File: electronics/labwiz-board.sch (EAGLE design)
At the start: 129 parts, among them IC1 MCP3424, J1 SD_MICRO_SDIO_1BIT, J2 CORTEX_DEBUGSMD, J30 4P-SMD-2.0-90D, J4 4P-SMD-2.0-90D, J5 4P-SMD-2.0-90D, U1 STM32F10XRXT6, U4 MIC5219-3.3V, X2 M12_BOTTOM_CONTACTS_FPC_1MM, Y1 32.768kHz, Y3 32.768kHz

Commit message: Added a header for USART1 Rx Tx.
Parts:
- added J43: (no value), SparkFun-Connectors:M02PTH
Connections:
- net USART1_RX: now also J43.2
- net USART1_TX: now also J43.1
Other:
- note added: "0.1.2-beta"
- note added: "BL-5C Batt"
- note added: "NOTES - Add labels to SWD pogo pads - Move the Cortex debug header to the right spot - Implement battery charging - VBAT_1/2 and SD_DETECT can reused as output if throw on some diodes."
- note removed: "0.13"
- note removed: "BL-5C Battery"
- note removed: "NOTES - Add labels to SWD pogo pads - Move the Cortex debug header to the right spot - Implement battery charging"
- note removed: "Orphan Nets"

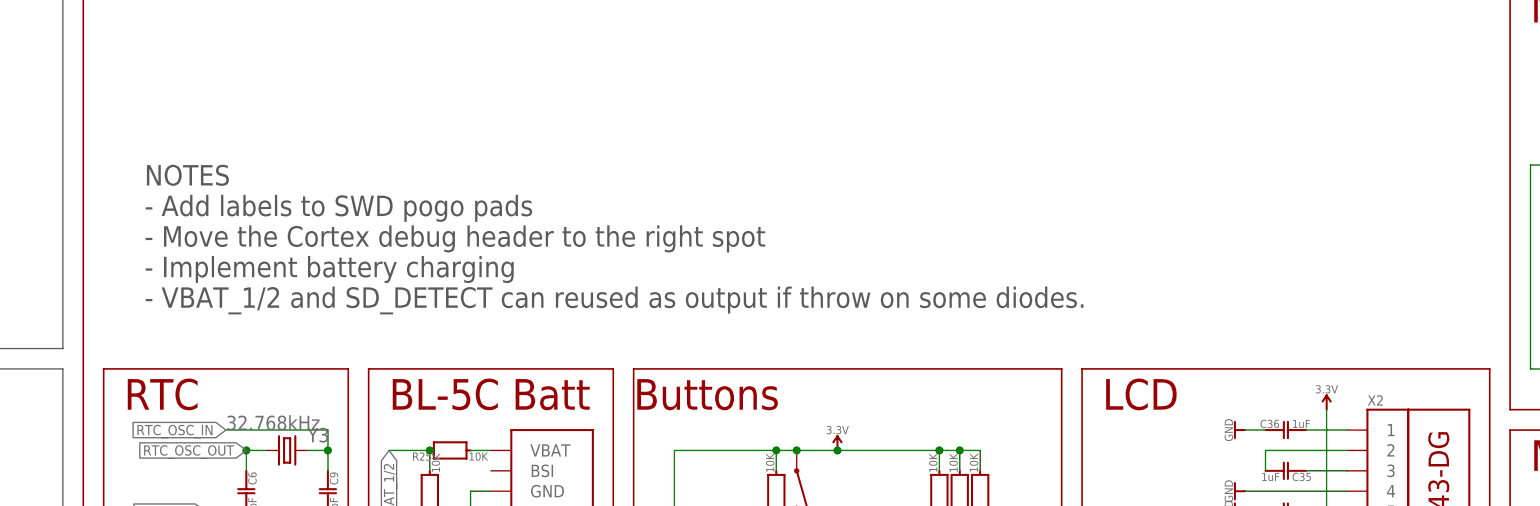
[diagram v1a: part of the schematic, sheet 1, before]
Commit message: Added pin docs to silk.
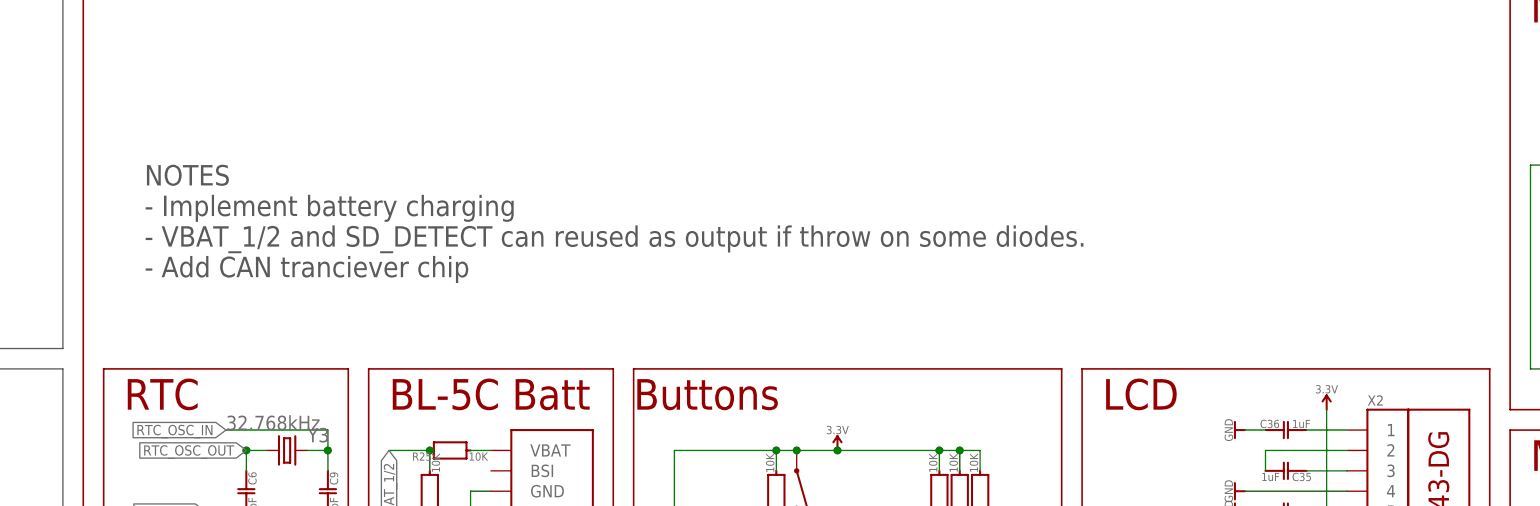
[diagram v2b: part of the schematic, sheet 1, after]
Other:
- note added: "NOTES - Implement battery charging - VBAT_1/2 and SD_DETECT can reused as output if throw on some diodes. - Add CAN tranciever chip"
- note removed: "NOTES - Add labels to SWD pogo pads - Move the Cortex debug header to the right spot - Implement battery charging - VBAT_1/2 and SD_DETECT can reused as output if throw on some diodes."
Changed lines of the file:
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@@
 <wire x1="289.56" y1="139.7" x2="381" y2="139.7" width="0.2032" layer="94"/>
 <text x="119.38" y="114.3" size="2.54" layer="97" align="top-left">NOTES
-- Add labels to SWD pogo pads
-- Move the Cortex debug header to the right spot
 - Implement battery charging
-- VBAT_1/2 and SD_DETECT can reused as output if throw on some diodes.</text>
+- VBAT_1/2 and SD_DETECT can reused as output if throw on some diodes.
+- Add CAN tranciever chip</text>
 <text x="193.04" y="22.86" size="1.27" layer="97" font="fixed" align="top-left">ESP01 Module
  TXO 2 1 GND

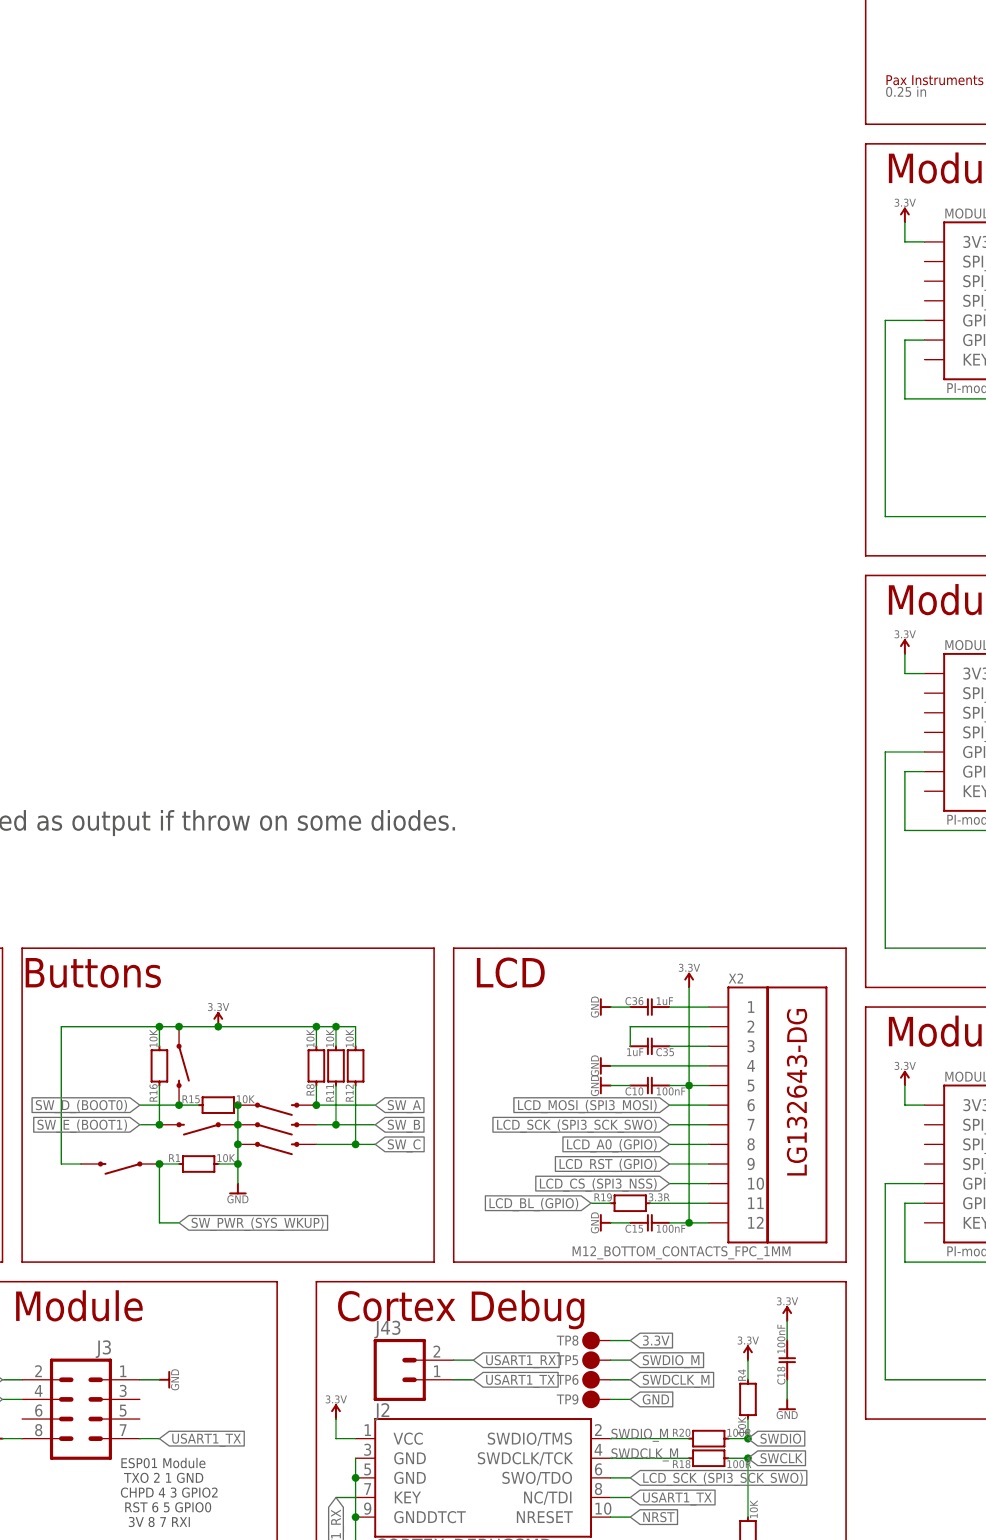
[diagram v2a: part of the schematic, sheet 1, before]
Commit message: Moved USART1. Added USART1 pullup resistors.
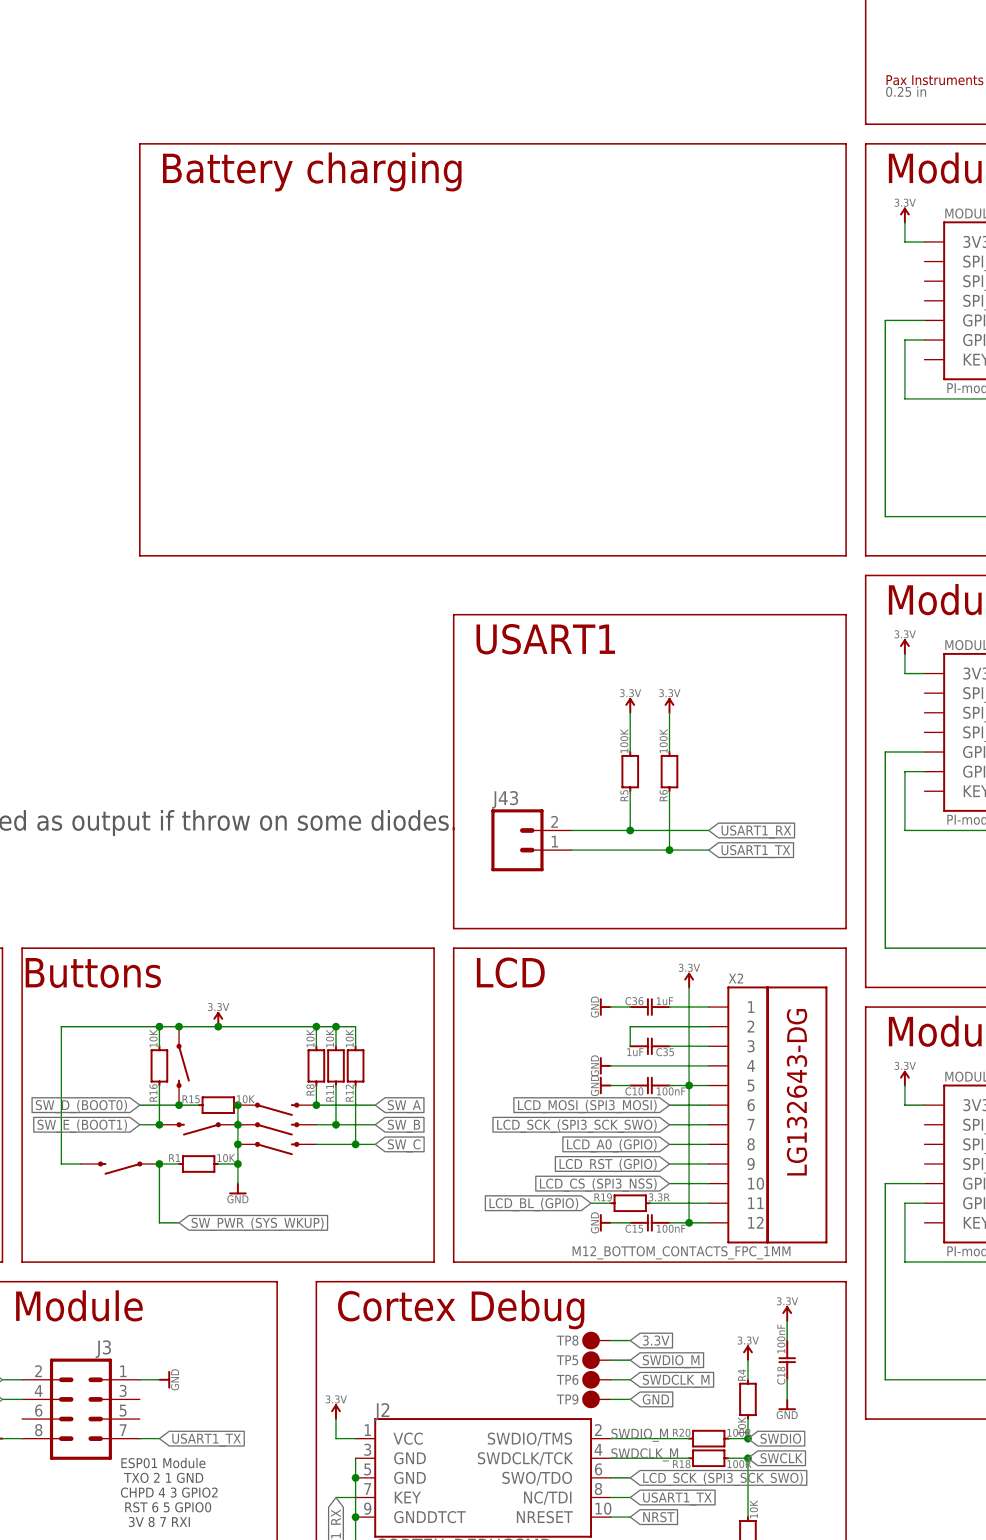
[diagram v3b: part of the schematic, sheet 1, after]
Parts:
- added R5, R6: 100K, PaxInstruments-RCL:R0402_10K
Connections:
- net 3.3V: now also R5.1, R6.1
- net USART1_RX: now also R5.2
- net USART1_TX: now also R6.2
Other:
- note added: "Battery charging"
- note added: "USART1"
- moved on the sheet: J43
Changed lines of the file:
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@@
 <part name="J42" library="SparkFun-Connectors" deviceset="M01" device="SMD-4.5X1.5"/>
 <part name="J43" library="SparkFun-Connectors" deviceset="M02" device="PTH"/>
+<part name="P+3" library="PaxInstruments-Aesthetics" deviceset="SYM_VCC" device="" technology="3.3V" value="3.3V"/>
+<part name="R5" library="PaxInstruments-RCL" deviceset="R0402" device="_10K" value="100K">
+<attribute name="MPN" value=""/>
+<attribute name="POPULATE" value=""/>
+</part>
+<part name="R6" library="PaxInstruments-RCL" deviceset="R0402" device="_10K" value="100K">
+<attribute name="MPN" value=""/>
+<attribute name="POPULATE" value=""/>
+</part>
+<part name="P+4" library="PaxInstruments-Aesthetics" deviceset="SYM_VCC" device="" technology="3.3V" value="3.3V"/>
 </parts>
 <sheets>
@@
 <circle x="378.46" y="43.18" radius="1.27" width="0.1524" layer="94"/>
 <circle x="378.46" y="45.72" radius="1.27" width="0.1524" layer="97"/>
+<wire x1="287.02" y1="139.7" x2="287.02" y2="193.04" width="0.2032" layer="94"/>
+<wire x1="195.58" y1="193.04" x2="287.02" y2="193.04" width="0.2032" layer="94"/>
+<wire x1="195.58" y1="139.7" x2="287.02" y2="139.7" width="0.2032" layer="94"/>
+<wire x1="195.58" y1="139.7" x2="195.58" y2="193.04" width="0.2032" layer="94"/>
+<text x="198.12" y="187.96" size="3.81" layer="94">Battery charging</text>
+<wire x1="236.22" y1="91.44" x2="287.02" y2="91.44" width="0.2032" layer="94"/>
+<wire x1="236.22" y1="91.44" x2="236.22" y2="132.08" width="0.2032" layer="94"/>
+<wire x1="287.02" y1="91.44" x2="287.02" y2="132.08" width="0.2032" layer="94"/>
+<wire x1="236.22" y1="132.08" x2="287.02" y2="132.08" width="0.2032" layer="94"/>
+<text x="238.76" y="127" size="3.81" layer="94">USART1</text>
 </plain>
 <instances>
@@
 <instance part="J41" gate="G$1" x="353.06" y="43.18"/>
 <instance part="J42" gate="G$1" x="353.06" y="33.02"/>
-<instance part="J43" gate="G$1" x="228.6" y="33.02"/>
+<instance part="J43" gate="G$1" x="243.84" y="101.6"/>
+<instance part="P+3" gate="G$1" x="264.16" y="119.38" rot="MR0"/>
+<instance part="R5" gate="G$1" x="259.08" y="111.76">
+<attribute name="MPN" x="259.08" y="111.76" size="1.778" layer="96" display="off"/>
+<attribute name="POPULATE" x="259.08" y="111.76" size="1.778" layer="96" display="off"/>
+</instance>
+<instance part="R6" gate="G$1" x="264.16" y="111.76">
+<attribute name="MPN" x="264.16" y="111.76" size="1.778" layer="96" display="off"/>
+<attribute name="POPULATE" x="264.16" y="111.76" size="1.778" layer="96" display="off"/>
+</instance>
+<instance part="P+4" gate="G$1" x="259.08" y="119.38" rot="MR0"/>
 </instances>
 <busses>
@@
 <wire x1="180.34" y1="25.4" x2="177.8" y2="25.4" width="0.1524" layer="91"/>
 <pinref part="SUPPLY12" gate="G$1" pin="3.3V"/>
+</segment>
+<segment>
+<pinref part="R5" gate="G$1" pin="1"/>
+<pinref part="P+4" gate="G$1" pin="3.3V"/>
+<wire x1="259.08" y1="114.3" x2="259.08" y2="119.38" width="0.1524" layer="91"/>
+</segment>
+<segment>
+<pinref part="R6" gate="G$1" pin="1"/>
+<pinref part="P+3" gate="G$1" pin="3.3V"/>
+<wire x1="264.16" y1="114.3" x2="264.16" y2="119.38" width="0.1524" layer="91"/>
 </segment>
 </net>
@@
 <segment>
 <pinref part="J43" gate="G$1" pin="1"/>
-<wire x1="236.22" y1="33.02" x2="238.76" y2="33.02" width="0.1524" layer="91"/>
-<label x="238.76" y="33.02" size="1.27" layer="95" xref="yes"/>
+<wire x1="251.46" y1="101.6" x2="264.16" y2="101.6" width="0.1524" layer="91"/>
+<label x="269.24" y="101.6" size="1.27" layer="95" xref="yes"/>
+<pinref part="R6" gate="G$1" pin="2"/>
+<wire x1="264.16" y1="101.6" x2="269.24" y2="101.6" width="0.1524" layer="91"/>
+<wire x1="264.16" y1="109.22" x2="264.16" y2="101.6" width="0.1524" layer="91"/>
+<junction x="264.16" y="101.6"/>
 </segment>
 </net>
@@
 <segment>
 <pinref part="J43" gate="G$1" pin="2"/>
-<wire x1="236.22" y1="35.56" x2="238.76" y2="35.56" width="0.1524" layer="91"/>
-<label x="238.76" y="35.56" size="1.27" layer="95" xref="yes"/>
-</segment>
-</net>
+<wire x1="251.46" y1="104.14" x2="259.08" y2="104.14" width="0.1524" layer="91"/>
+<label x="269.24" y="104.14" size="1.27" layer="95" xref="yes"/>
+<pinref part="R5" gate="G$1" pin="2"/>
+<wire x1="259.08" y1="104.14" x2="269.24" y2="104.14" width="0.1524" layer="91"/>
+<wire x1="259.08" y1="109.22" x2="259.08" y2="104.14" width="0.1524" layer="91"/>
+<junction x="259.08" y="104.14"/>
+</segment>
+</net>

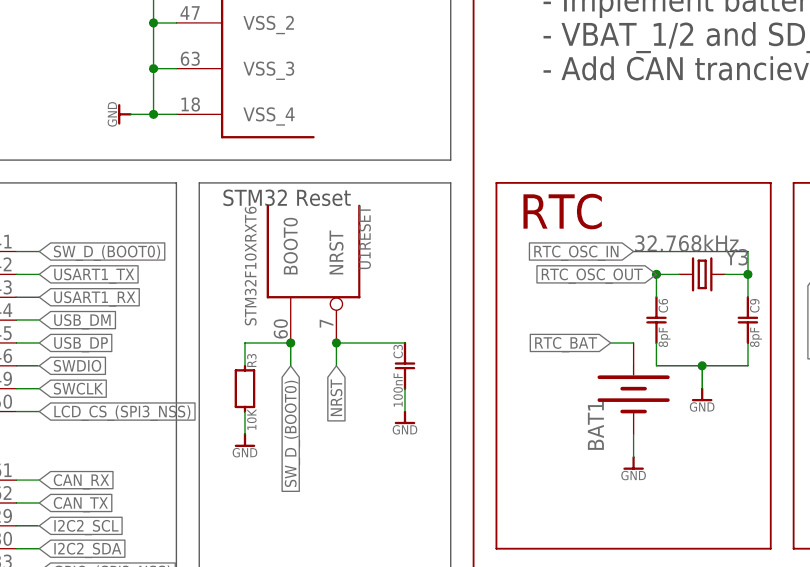
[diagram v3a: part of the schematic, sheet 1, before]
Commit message: Added pullup to RESET.
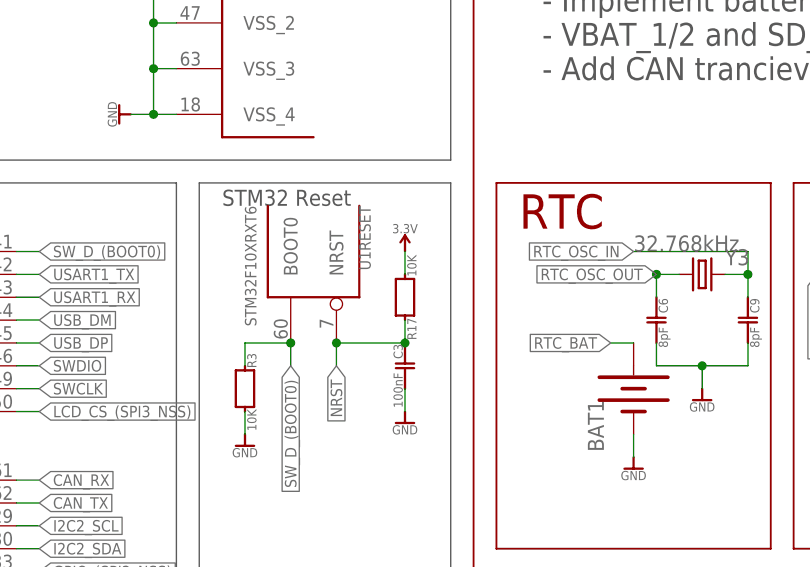
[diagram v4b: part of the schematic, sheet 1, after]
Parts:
- added R17: 10K, PaxInstruments-RCL:R0402_10K
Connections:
- net 3.3V: now also R17.1
- net NRST: now also R17.2
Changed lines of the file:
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@@
 </part>
 <part name="P+4" library="PaxInstruments-Aesthetics" deviceset="SYM_VCC" device="" technology="3.3V" value="3.3V"/>
+<part name="R17" library="PaxInstruments-RCL" deviceset="R0402" device="_10K" value="10K"/>
+<part name="SUPPLY23" library="PaxInstruments-Aesthetics" deviceset="SYM_VCC" device="" technology="3.3V" value="3.3V"/>
 </parts>
 <sheets>
@@
 </instance>
 <instance part="P+4" gate="G$1" x="259.08" y="119.38" rot="MR0"/>
+<instance part="R17" gate="G$1" x="104.14" y="76.2" rot="MR0"/>
+<instance part="SUPPLY23" gate="G$1" x="104.14" y="81.28"/>
 </instances>
 <busses>
@@
 <pinref part="P+3" gate="G$1" pin="3.3V"/>
 <wire x1="264.16" y1="114.3" x2="264.16" y2="119.38" width="0.1524" layer="91"/>
+</segment>
+<segment>
+<pinref part="R17" gate="G$1" pin="1"/>
+<pinref part="SUPPLY23" gate="G$1" pin="3.3V"/>
+<wire x1="104.14" y1="78.74" x2="104.14" y2="81.28" width="0.1524" layer="91"/>
 </segment>
 </net>
@@
 <wire x1="104.14" y1="71.12" x2="96.52" y2="71.12" width="0.1524" layer="91"/>
 <junction x="96.52" y="71.12"/>
-</segment>
-<segment>
+<pinref part="R17" gate="G$1" pin="2"/>
+<wire x1="104.14" y1="71.12" x2="104.14" y2="73.66" width="0.1524" layer="91"/>
+<junction x="104.14" y="71.12"/>
+</segment>
+<segment>
